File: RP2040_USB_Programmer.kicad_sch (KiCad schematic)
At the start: 24 parts, among them J3 TSM-104-01-L-SV, SW1 1825910-6, U5 RP2040, U6 W25Q16JVSSIQ, X1 X322512MSB4SI

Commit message: Finished STM32 Stage
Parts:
- renumbered C9 to C10, C10 to C11, C11 to C12, C4 to C15, C5 to C16, C12 to C7, C7 to C8, C8 to C9, R20 to R18, R21 to R19, R23 to R20, R22 to R21, R19 to R22, R18 to R23

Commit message: - Added Hysteresis resistor on TLV431BSN1T1G - Lowered TLV431BSN1T1G impedance values for resistors on the voltage divider
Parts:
- BOOT_SEL1: renamed from S1; footprint SS12D07VG4:SW_SS12D07VG4 -> BOOT toggle switch - SS12D07VG4 087:SW_SS12D07VG4
- J3: footprint TSM-104-01-L-SV:SAMTEC_TSM-104-01-L-SV -> Samtec TSM-104-01-L-SV:SAMTEC_TSM-104-01-L-SV
- OV_LED2: renamed from OV LED2; footprint LED-SMD-RED-DIFFUSED_0603_:LED-0603 -> RED LED Indicator - LED-SMD-RED-DIFFUSED_0603:LED-0603
- SW_RESET1: renamed from SW1; footprint 1825910-6:SW_1825910-6-4 -> RP RST - Button - 1825910-6:SW_1825910-6-4
- U5: renamed from U6; footprint W25Q16JVSSIQ:SOIC127P790X216-8N -> Flash for RP - W25Q16JVSSIQ:SOIC127P790X216-8N
- renumbered C8 to C10, C9 to C11, C10 to C12, C11 to C13, C12 to C14, C13 to C15, C14 to C16, C15 to C17, C16 to C18, C6 to C8, C7 to C9, U5 to U4
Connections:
- net GND: now also C13.2; no longer C13.1
- net RP2040_SWDIO: no longer J3.02, U4.25 (SWD)
- net SYS_3V3: now also C13.1; no longer C13.2
- net at J3.01: now also U4.25 (SWD); no longer U4.24 (SWCLK)
- net USB_DM renamed USB_D-
- net USB_DP renamed USB_D+
- new net: J3.02, U4.24 (SWCLK)
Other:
- company: Yaniv Lieberman -> (none)
- title: (none) -> Integrated Si5351A Module - USB Programmer Stage
- moved on the sheet: C13, J3

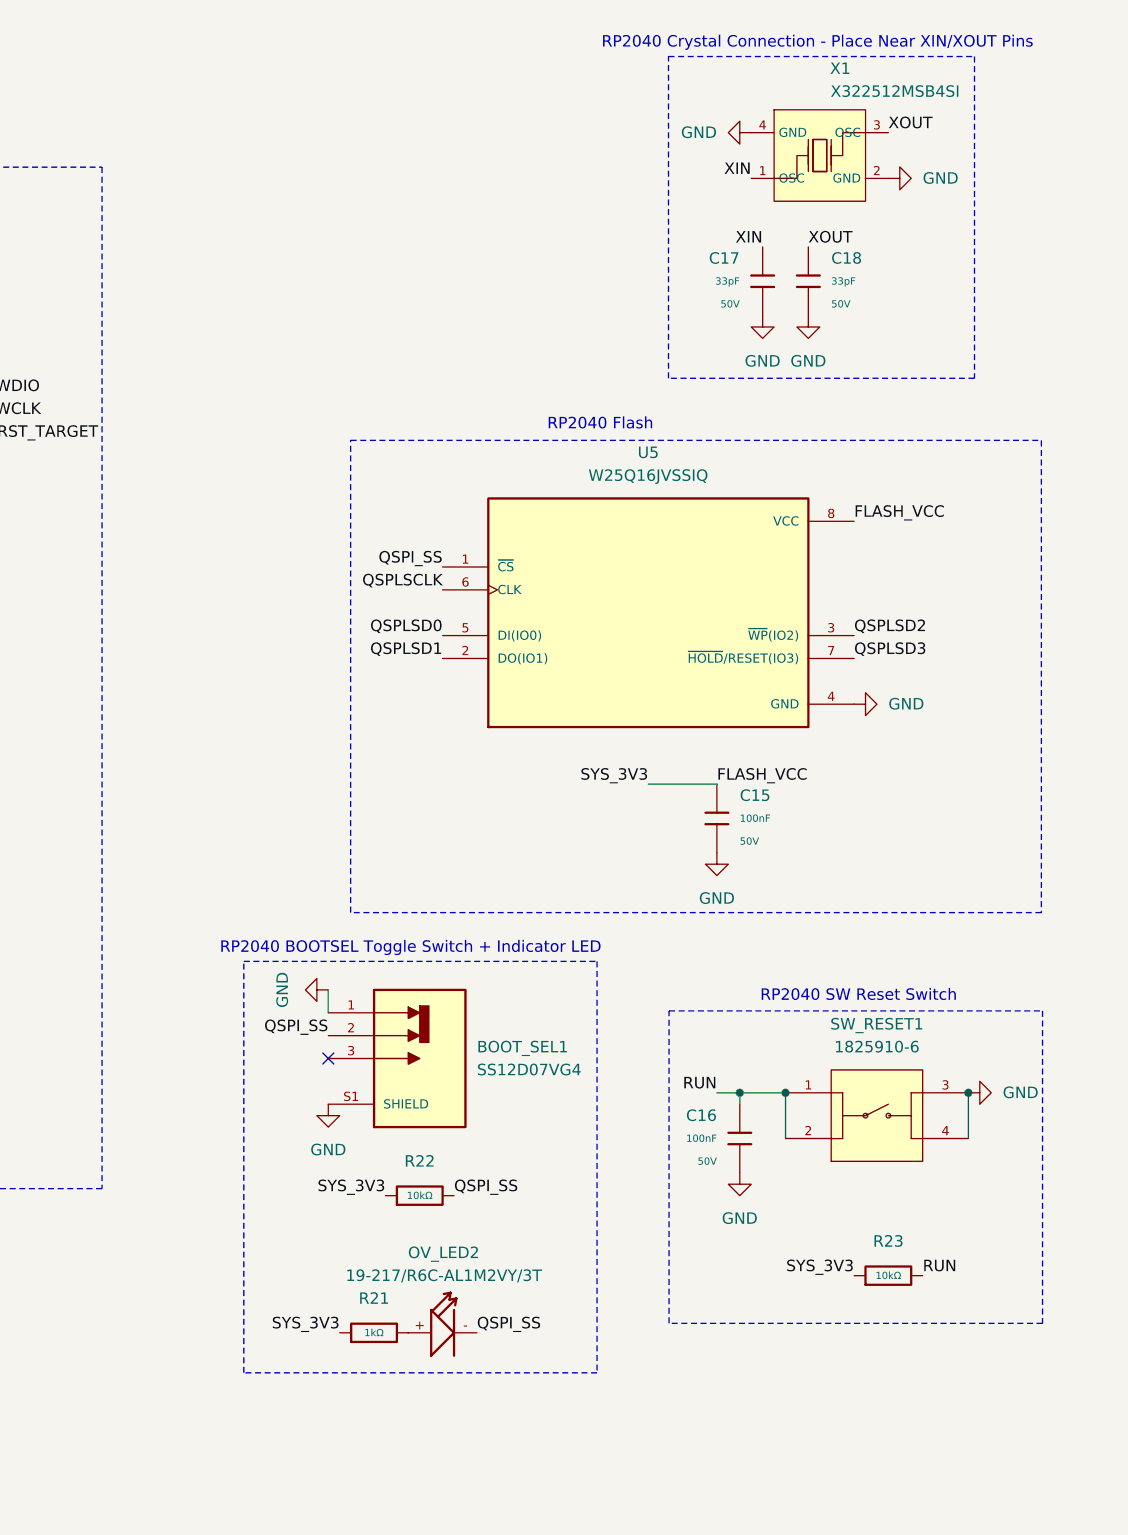
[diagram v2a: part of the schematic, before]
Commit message: -Added bouncing prevention capacitor on BOOT_SEL
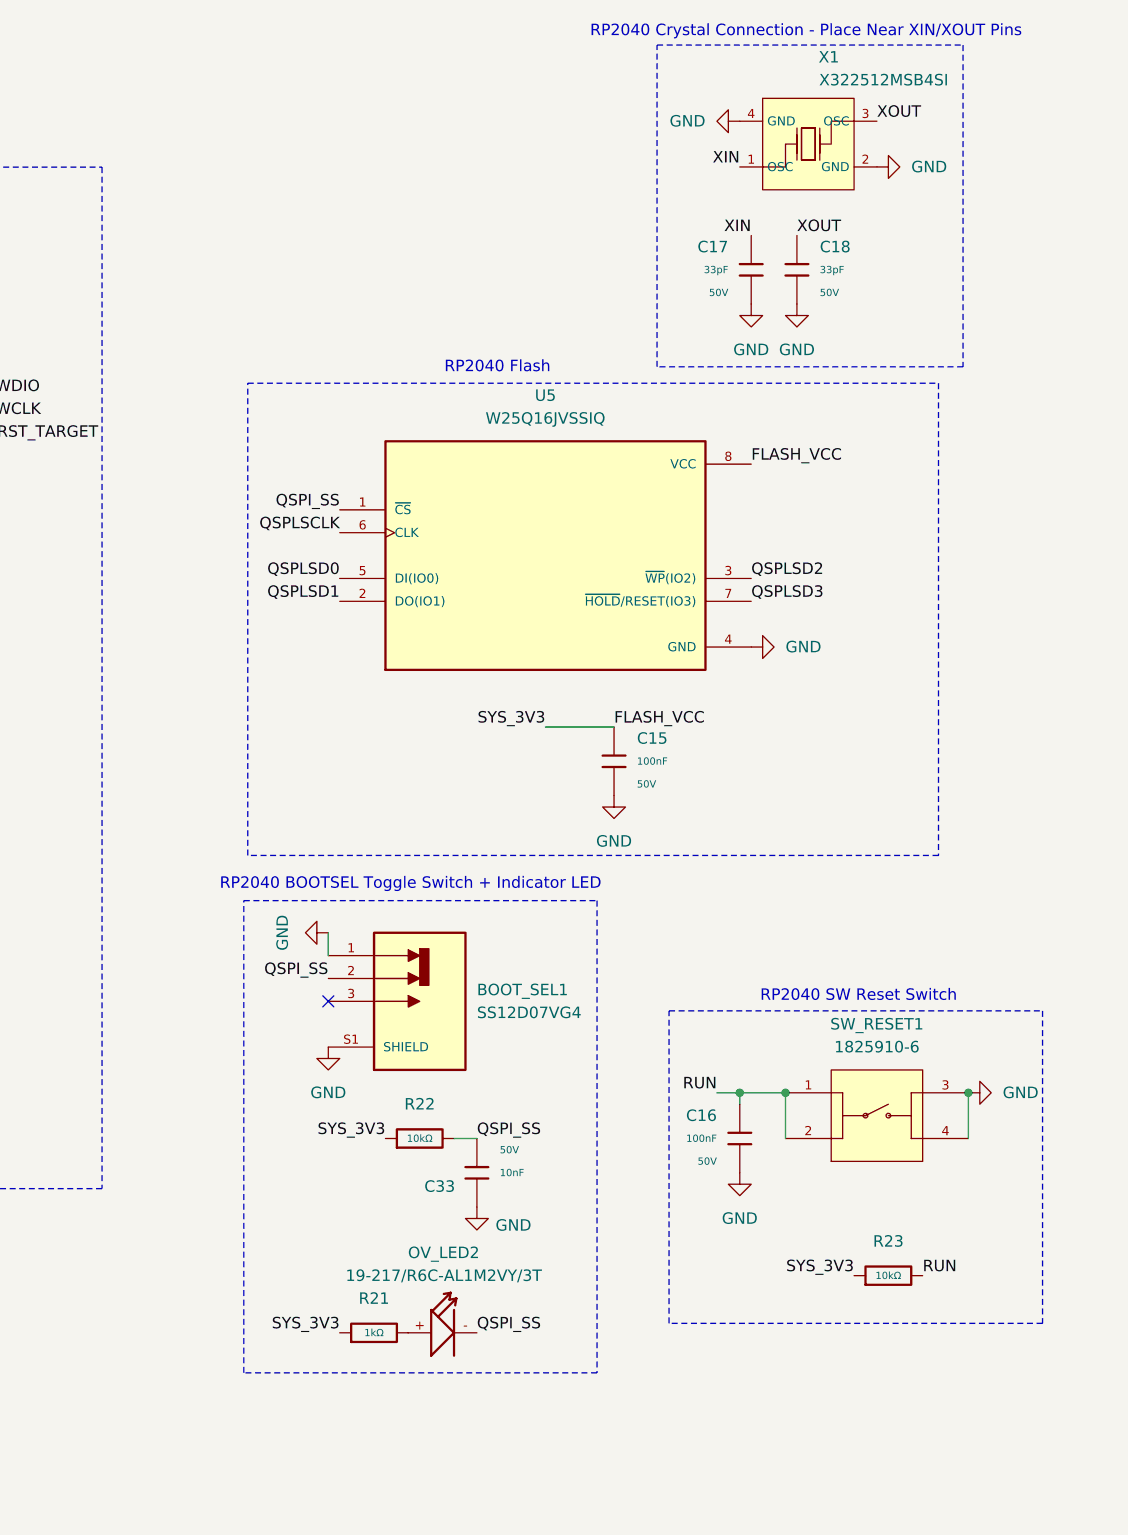
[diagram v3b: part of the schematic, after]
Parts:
- added C33: 10nF, PCM_JLCPCB:C_0603, symbol PCM_JLCPCB-Capacitors:0603,100nF
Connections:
- net GND: now also C33.2
- net QSPI_SS: now also C33.1
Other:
- moved on the sheet: BOOT_SEL1, C15, C17, C18, R22, U5, X1
